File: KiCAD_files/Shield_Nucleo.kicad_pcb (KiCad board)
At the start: 4 copper layers, 100 x 100 mm, 132 parts, among them J1 Conn_01x02, J2 RJ45_LED_Shielded, J3 RJ45_LED_Shielded, J4 Conn_01x03_Male, J5 Conn_01x05_Male, J6 Conn_01x02, J7 Power, J8 Conn_02x07_Odd_Even, J9 Conn_01x03, SW1 SW_Push, U1 STM32G474RE, U10 MCP1799T-5002H/TT, U2 AT25xxx, U3 TCAN334GDR, U4 AP1117-33, U5 UCC21222DR, U6 UCC21222DR, U7 SFH617A-2X009T, U8 RFM-0505s, U9 CME0512S3C, Y1 ECS-240-10-33-AGM-TR - 24MHz

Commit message: Added gerbers files used for PCB order
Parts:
- J4: value Conn_01x03_Male -> Conn_01x06_Male; footprint Connector_PinHeader_2.54mm:PinHeader_1x03_P2.54mm_Vertical -> Connector_PinHeader_2.54mm:PinHeader_1x06_P2.54mm_Vertical
- J5: value Conn_01x05_Male -> Conn_01x06_Male; footprint Connector_PinHeader_2.54mm:PinHeader_1x05_P2.54mm_Vertical -> Connector_PinHeader_2.54mm:PinHeader_1x06_P2.54mm_Vertical
- moved J4 6.50 mm to (51.5, 61.3)
- moved J5 0.70 mm to (51.5, 77.5)
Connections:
- J4 pad 1: GNDD -> +3V3
- J4 pad 2: /USART1_TX -> /DTR
- J5 pad 1: /SPI3_MISO -> GNDD
- J5 pad 2: /SPI3_MOSI -> +3V3
- J5 pad 3: /SPI3_SCK -> /SPI3_MISO
- J5 pad 4: /SPI3_CS2 -> /SPI3_MOSI
- J5 pad 5: GNDD -> /SPI3_SCK
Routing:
- net +5VD: track 73.8 -> 108.8 mm
- net /GND_CAN: track 106.6 -> 85.4 mm
- net /USART1_RX: track 43.5 -> 55.0 mm
- net GNDREF: track 120.7 -> 114.2 mm
- net /USART1_TX: track 46.9 -> 52.6 mm
- net /SPI3_MOSI: track 74.9 -> 72.4 mm
- net /SPI3_SCK: track 82.5 -> 80.4 mm
- net Net-(JP1-Pad2): track 2.67 -> 1.09 mm
- net /HRTIM1_CHB1: track 41.8 -> 41.0 mm
- net /SPI3_MISO: track 71.7 -> 71.0 mm

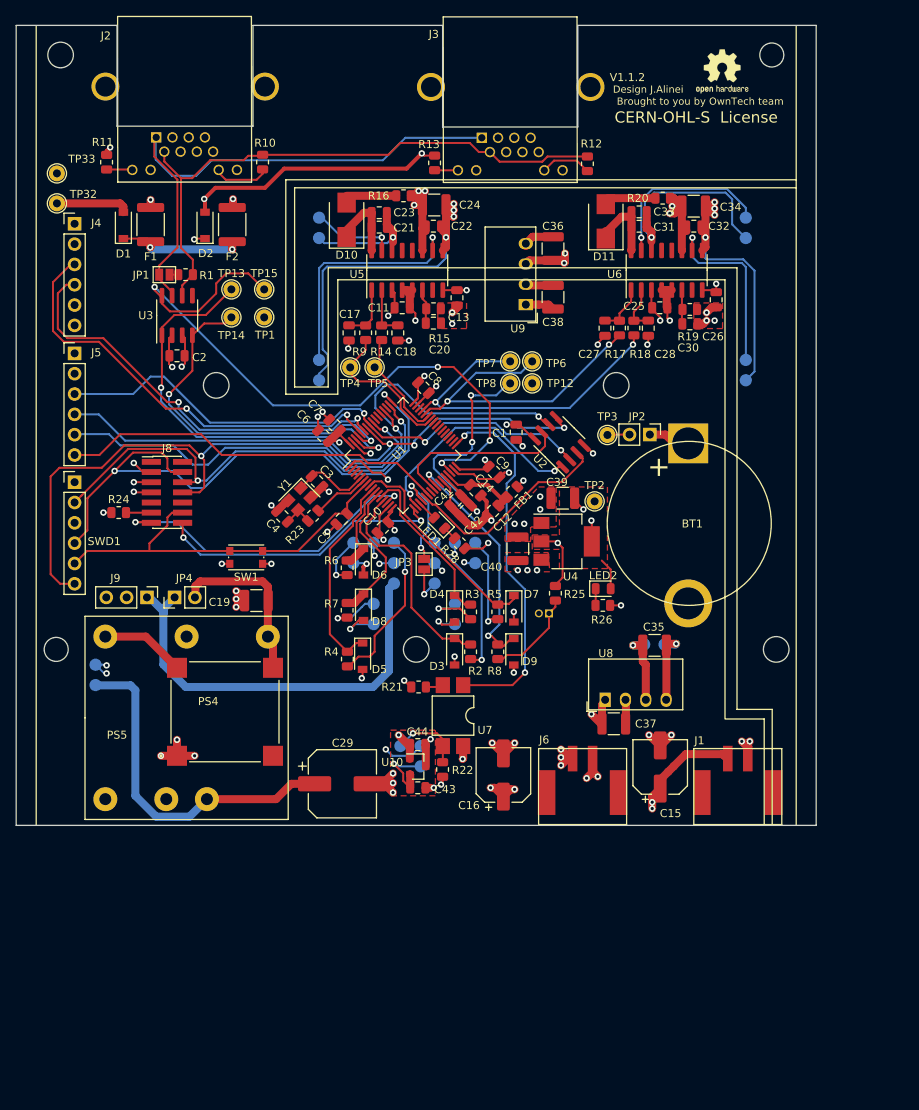
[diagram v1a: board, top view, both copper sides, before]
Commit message: Added a user comment layer on the control board for interface documentation
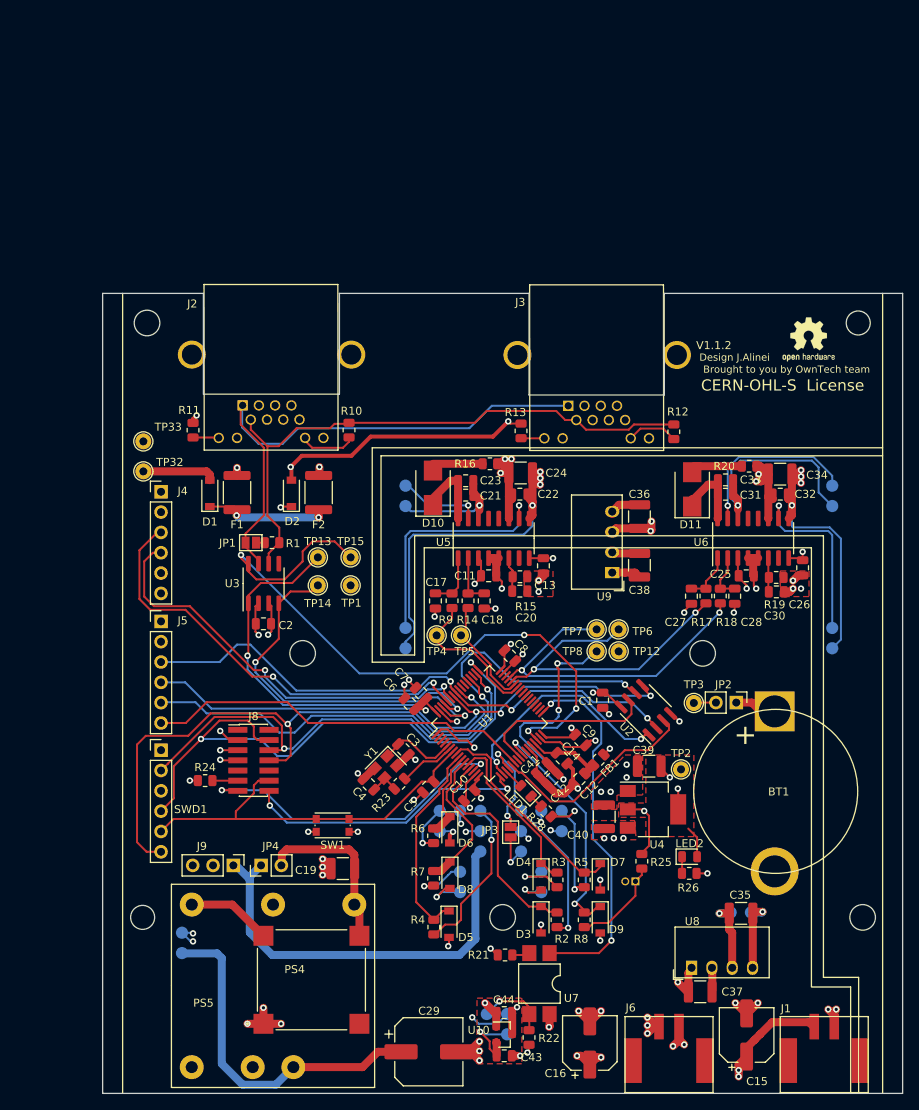
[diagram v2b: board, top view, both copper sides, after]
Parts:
- moved C1 35.2 mm to (117.5, 120.9)
- moved C10 35.2 mm to (100.8, 132.8)
- moved C11 35.2 mm to (103.3, 105.3)
- moved C13 35.2 mm to (110.1, 104.1)
- moved C14 35.2 mm to (112.4, 128.1)
- moved C16 35.2 mm to (115.9, 163.7)
- moved C17 35.2 mm to (96.6, 108.4)
- moved C19 35.2 mm to (85.0, 141.9)
- moved C2 35.2 mm to (75.1, 111.3)
- moved C20 35.2 mm to (107.2, 107.2)
- moved C21 35.2 mm to (100.4, 95.2)
- moved C25 35.2 mm to (135.5, 105.3)
- moved C26 35.2 mm to (142.5, 104.3)
- moved C27 35.2 mm to (128.6, 107.9)
- moved C28 35.2 mm to (134.0, 107.9)
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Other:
- board text added: "+3.3V"
- board text added: "+5VD"
- board text added: "+V CAN BUS"
- board text added: "2.048V"
- board text added: "3.3V"
- board text added: "5V EXT"
- board text added: "5V JP"
- board text added: "CAN1 STB"
- board text added: "DTR"
- board text added: "FDCAN RX"
- board text added: "FDCAN TX"
- board text added: "GND CAN"
- board text added: "GNDD"
- board text added: "NRST"
- board text added: "PWMH1"
- board text added: "PWMH2"
- board text added: "PWML1"
- board text added: "PWML2"
- board text added: "RST"
- board text added: "SPI3 CLK"
- board text added: "SPI3 CS2"
- board text added: "SPI3 MISO"
- board text added: "SPI3 MOSI"
- board text added: "STDC14"
- board text added: "SWCLK"
- board text added: "SWDIO"
- board text added: "SWO"
- board text added: "USART1_RX"
- board text added: "USART1_TX"
- board text added: "VBAT"
